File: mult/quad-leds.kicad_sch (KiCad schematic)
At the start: 14 parts, among them U5 LM324

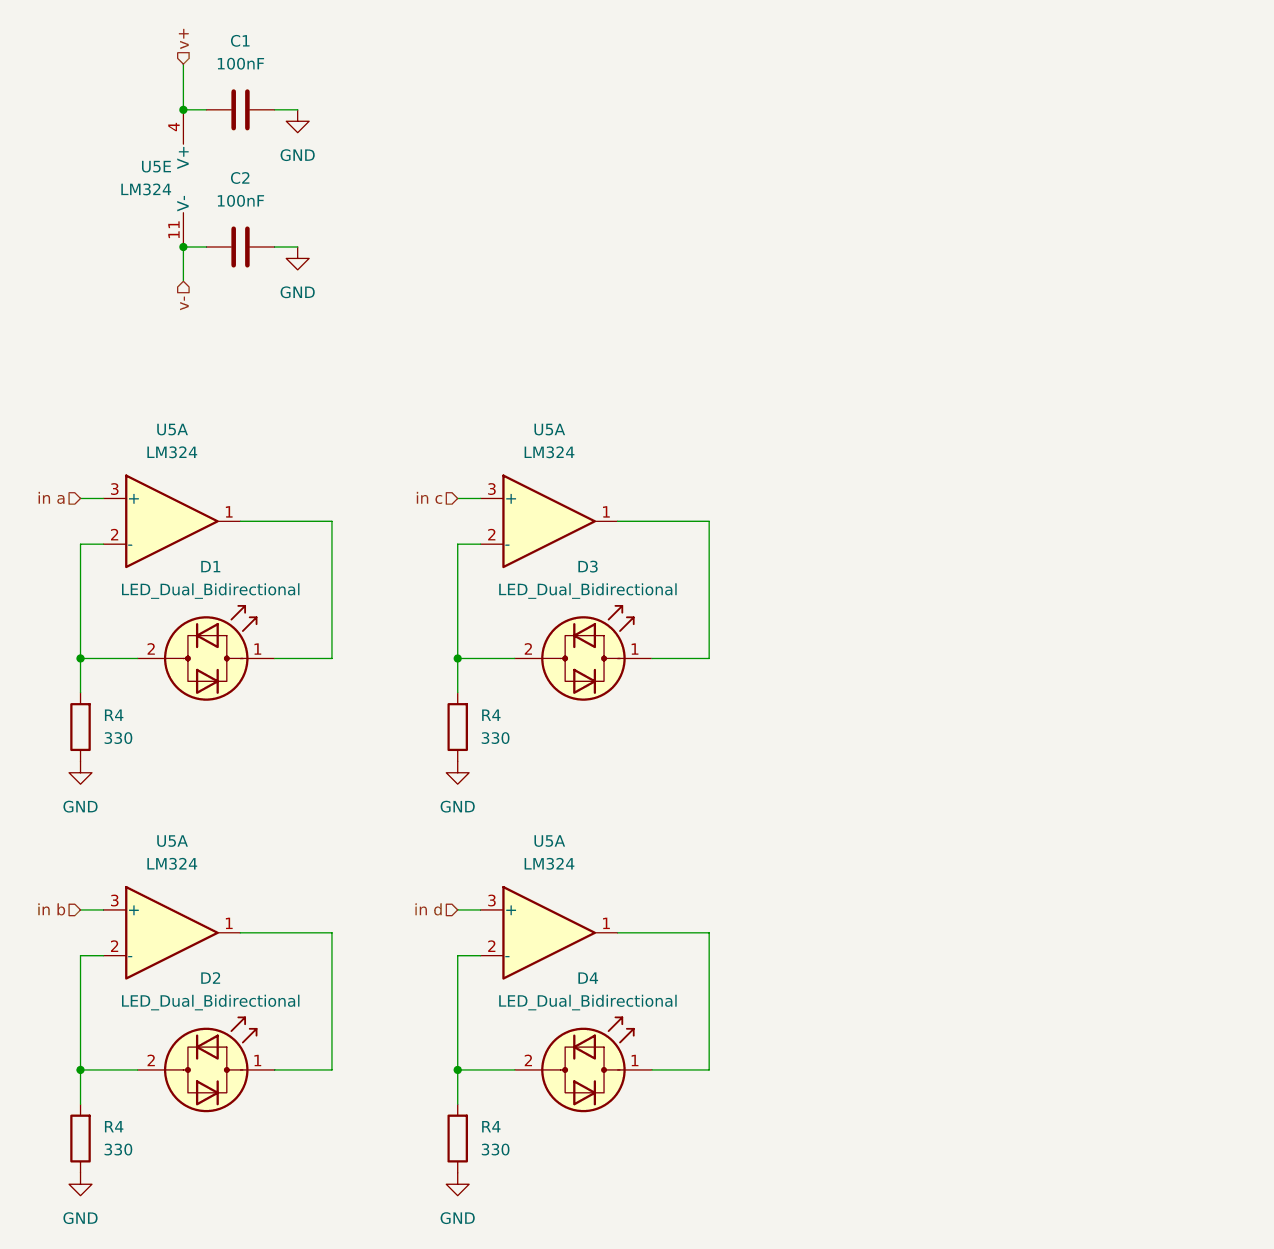
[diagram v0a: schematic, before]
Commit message: mult: Add LED TODOs, change resistor values to 680
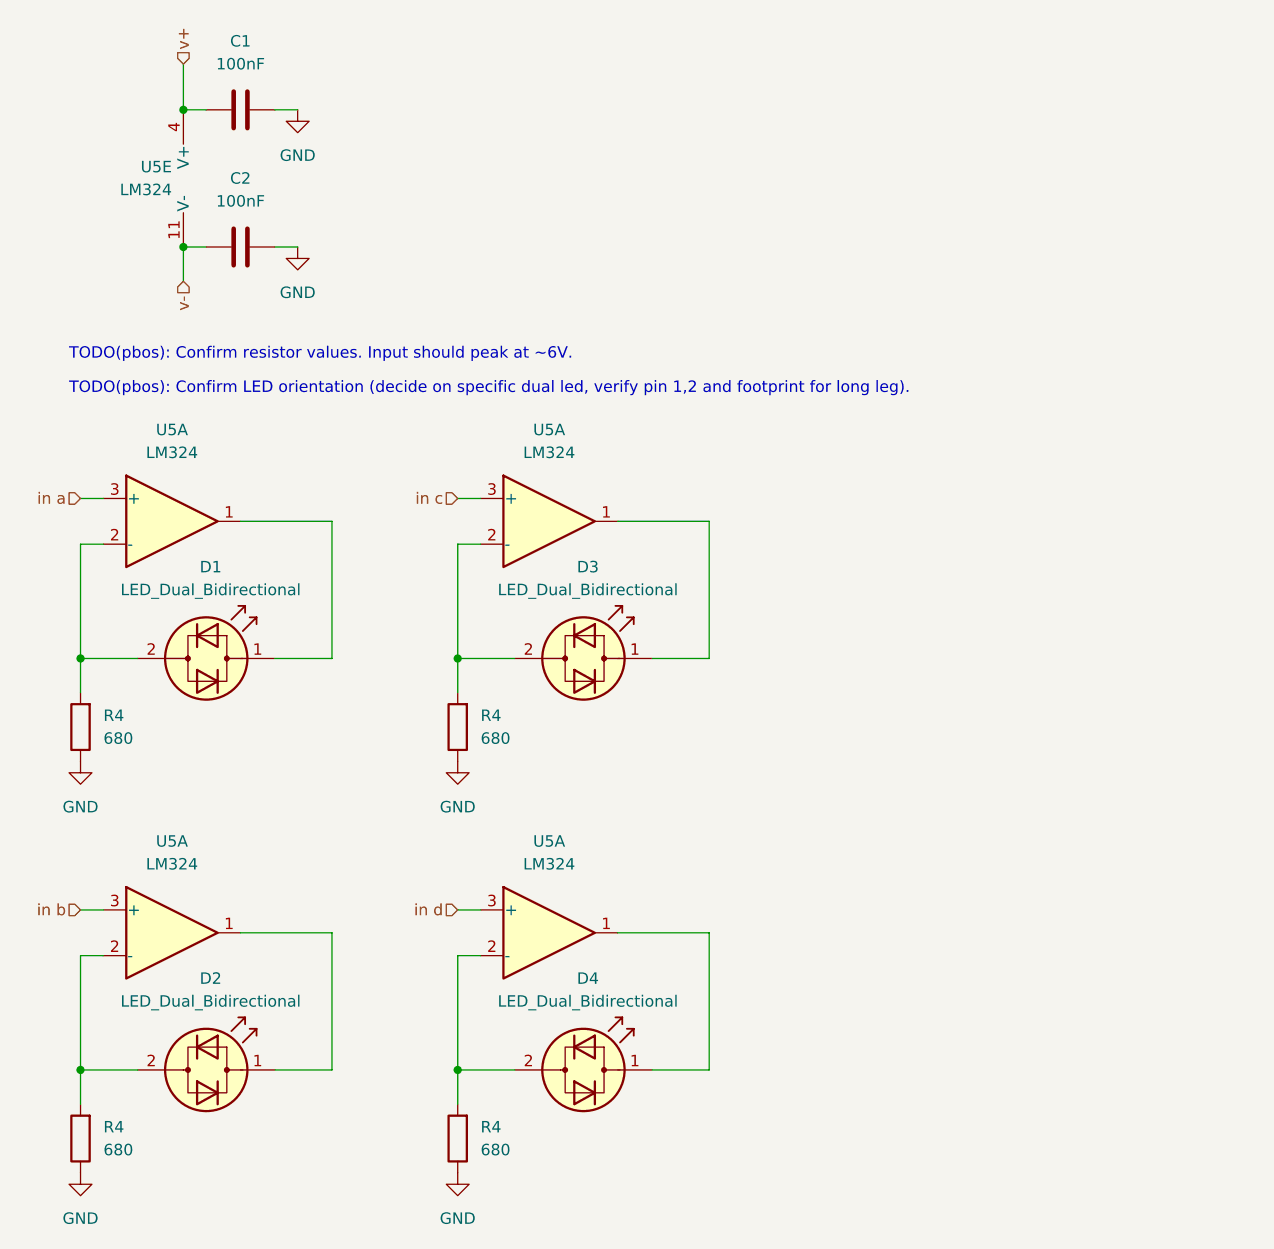
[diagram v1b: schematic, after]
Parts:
- R4: value 330 -> 680
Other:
- note added: "TODO(pbos): Confirm LED orientation (decide on specific dual led, verify pin 1,2 and footprint for long leg)."
- note added: "TODO(pbos): Confirm resistor values. Input should peak at ~6V."
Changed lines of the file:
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@@
     (stroke (width 0) (type default))
+  )
+  (text "TODO(pbos): Confirm LED orientation (decide on specific dual led, verify pin 1,2 and footprint for long leg)."
+    (at 78.74 73.66 0)
+    (effects (font (size 1.27 1.27)) (justify left bottom))
+  )
+  (text "TODO(pbos): Confirm resistor values. Input should peak at ~6V."
+    (at 78.74 69.85 0)
+    (effects (font (size 1.27 1.27)) (justify left bottom))
   )
   (hierarchical_label "in d" (shape input) (at 121.92 130.81 180) (fields_autoplaced)
@@
       (effects (font (size 1.27 1.27)) (justify right))
     )
-    (property "Value" "330" (at 82.55 157.48 0)
+    (property "Value" "680" (at 82.55 157.48 0)
       (effects (font (size 1.27 1.27)) (justify right))
     )
@@
       (effects (font (size 1.27 1.27)) (justify right))
     )
-    (property "Value" "330" (at 82.55 111.76 0)
+    (property "Value" "680" (at 82.55 111.76 0)
       (effects (font (size 1.27 1.27)) (justify right))
     )
@@
       (effects (font (size 1.27 1.27)) (justify right))
     )
-    (property "Value" "330" (at 124.46 157.48 0)
+    (property "Value" "680" (at 124.46 157.48 0)
       (effects (font (size 1.27 1.27)) (justify right))
     )
@@
       (effects (font (size 1.27 1.27)) (justify right))
     )
-    (property "Value" "330" (at 124.46 111.76 0)
-      (effects (font (size 1.27 1.27)) (justify right))
-    )
+    (property "Value" "680" (at 124.46 111.76 0)
+      (effects (font (size 1.27 1.27)) (justify right))
+    )

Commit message: mult: Add TSSOP footprint to LM324
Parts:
- U5: footprint (none) -> Package_SO:TSSOP-14_4.4x5mm_P0.65mm
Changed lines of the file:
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@@
       (effects (font (size 1.27 1.27)))
     )
-    (property "Footprint" "" (at 130.81 130.81 0)
+    (property "Footprint" "Package_SO:TSSOP-14_4.4x5mm_P0.65mm" (at 130.81 130.81 0)
       (effects (font (size 1.27 1.27)) hide)
     )
@@
       (effects (font (size 1.27 1.27)))
     )
-    (property "Footprint" "" (at 88.9 85.09 0)
+    (property "Footprint" "Package_SO:TSSOP-14_4.4x5mm_P0.65mm" (at 88.9 85.09 0)
       (effects (font (size 1.27 1.27)) hide)
     )
@@
       (effects (font (size 1.27 1.27)))
     )
-    (property "Footprint" "" (at 130.81 85.09 0)
+    (property "Footprint" "Package_SO:TSSOP-14_4.4x5mm_P0.65mm" (at 130.81 85.09 0)
       (effects (font (size 1.27 1.27)) hide)
     )
@@
       (effects (font (size 1.27 1.27)) (justify left))
     )
-    (property "Footprint" "" (at 90.17 46.99 0)
+    (property "Footprint" "Package_SO:TSSOP-14_4.4x5mm_P0.65mm" (at 90.17 46.99 0)
       (effects (font (size 1.27 1.27)) hide)
     )
@@
       (effects (font (size 1.27 1.27)))
     )
-    (property "Footprint" "" (at 88.9 130.81 0)
-      (effects (font (size 1.27 1.27)) hide)
-    )
+    (property "Footprint" "Package_SO:TSSOP-14_4.4x5mm_P0.65mm" (at 88.9 130.81 0)
+      (effects (font (size 1.27 1.27)) hide)
+    )

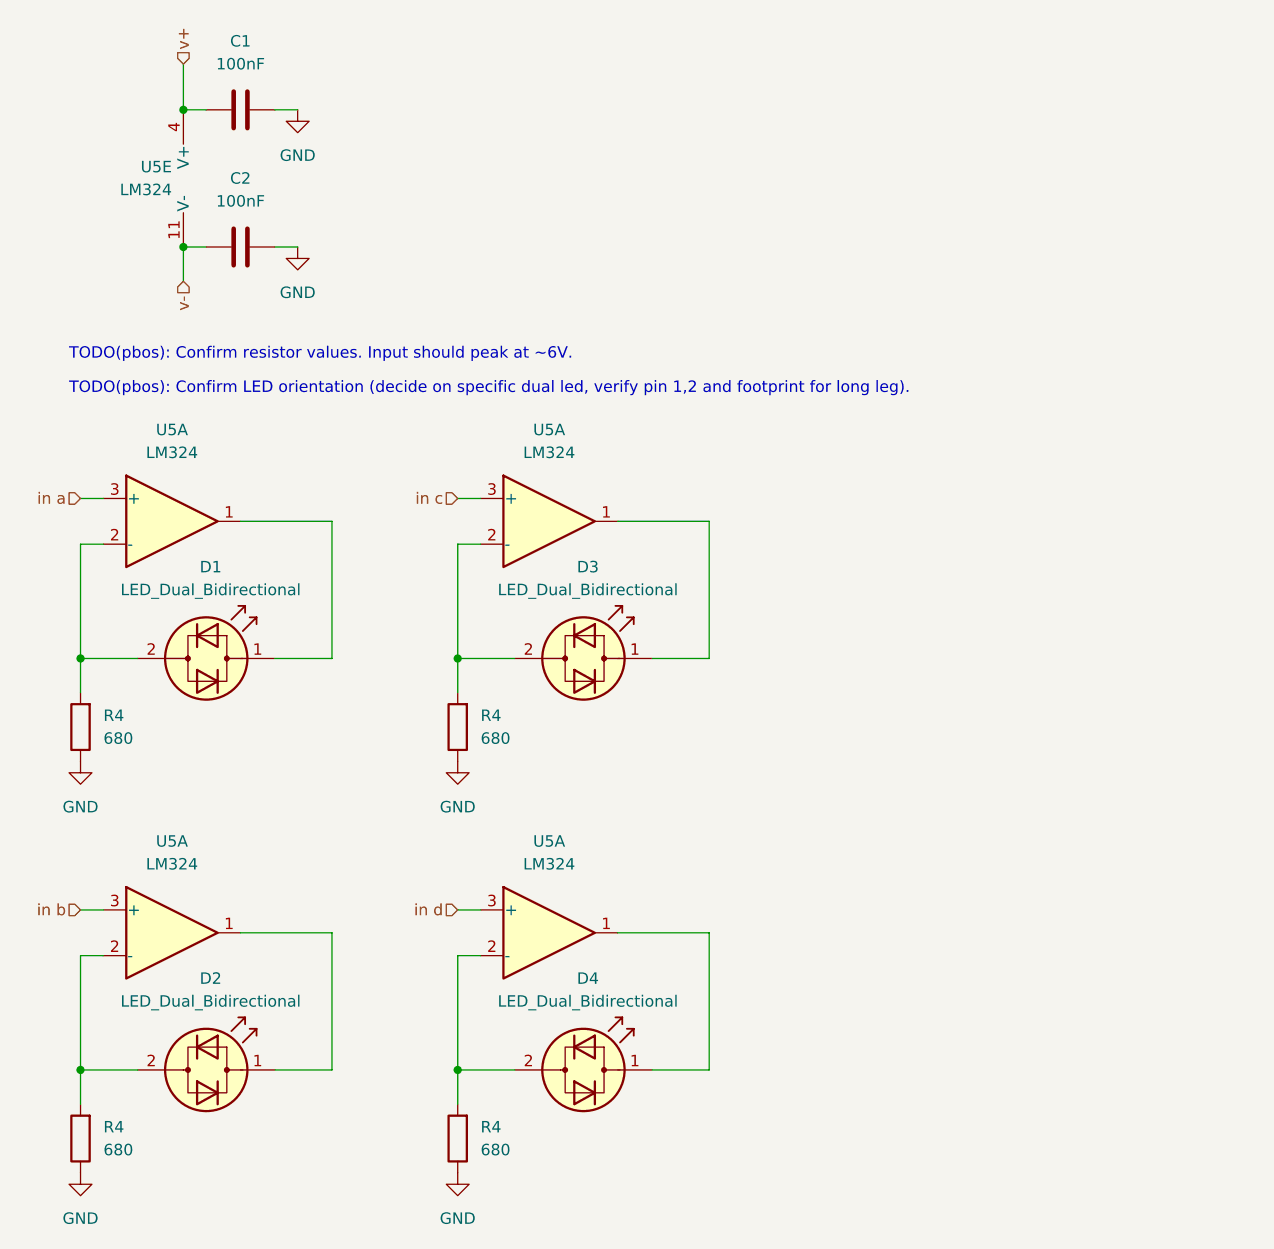
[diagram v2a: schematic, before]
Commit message: mult: Replace v+ and v- labels with VCC,VEE
This removes a lot of unnecessary wires as well. Also updating LED
resistors to 1k to match Mutable Instruments Links and resolving TODO.
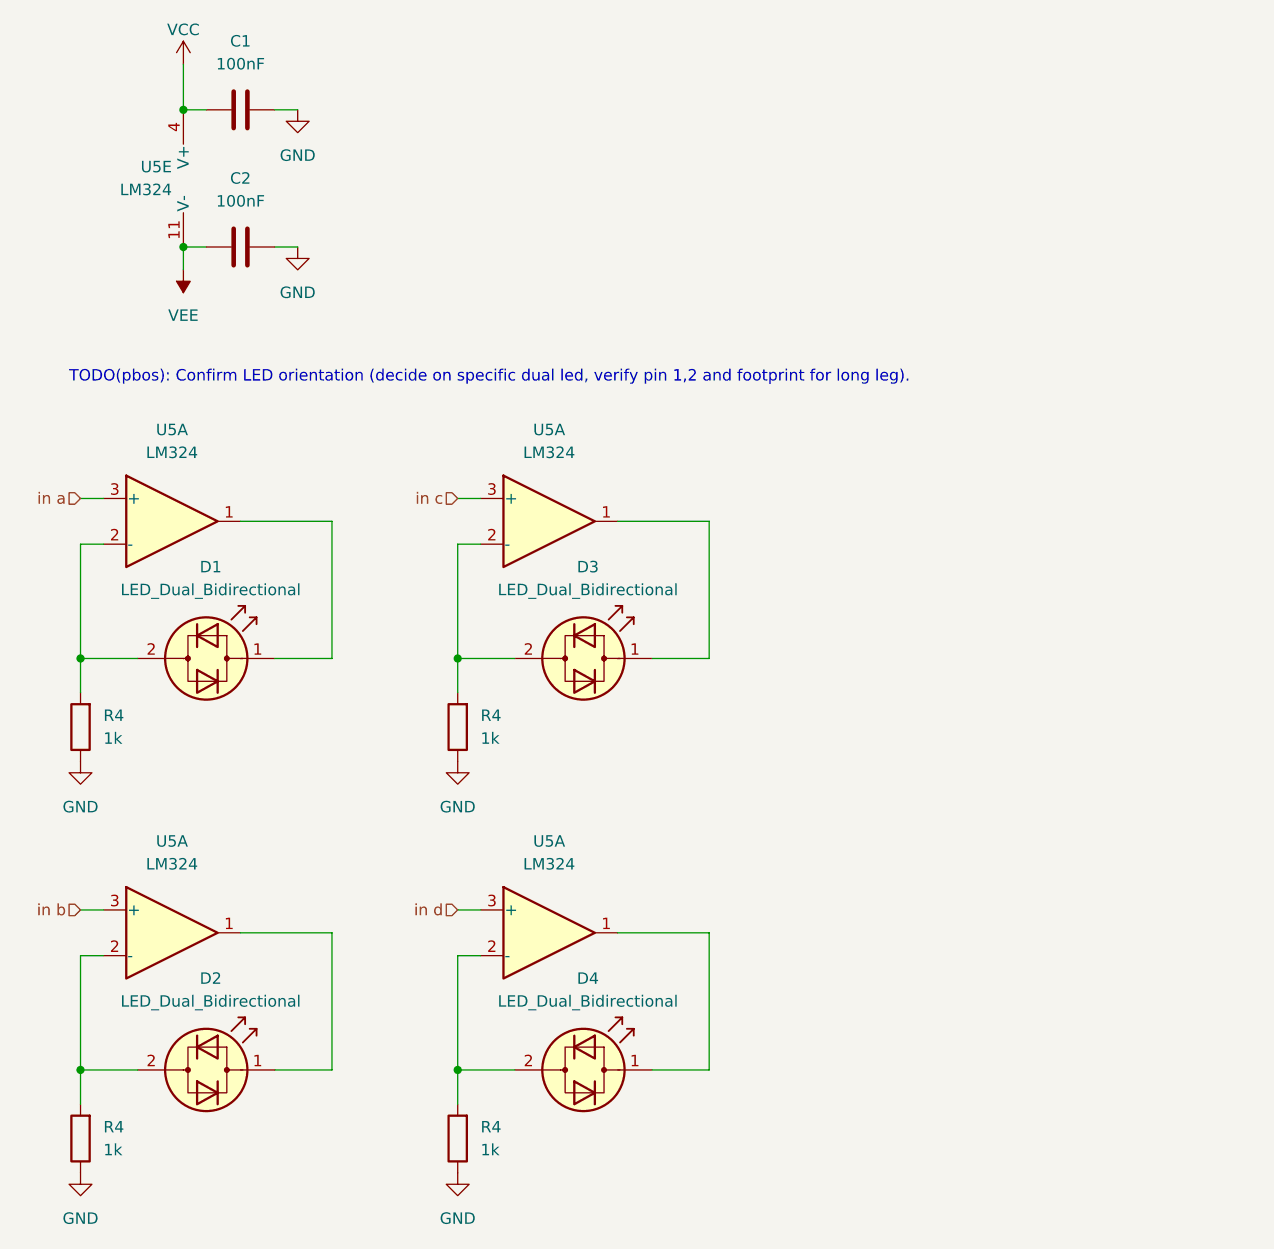
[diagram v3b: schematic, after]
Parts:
- R4: value 680 -> 1k
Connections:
- net v+ renamed VCC
- net v- renamed VEE
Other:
- note removed: "TODO(pbos): Confirm resistor values. Input should peak at ~6V."
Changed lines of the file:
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@@
     (stroke (width 0) (type default))
   )
-  (wire (pts (xy 91.44 60.96) (xy 91.44 57.15))
+  (wire (pts (xy 91.44 59.69) (xy 91.44 57.15))
     (stroke (width 0) (type default))
   )
@@
   )
   (text "TODO(pbos): Confirm LED orientation (decide on specific dual led, verify pin 1,2 and footprint for long leg)."
-    (at 78.74 73.66 0)
-    (effects (font (size 1.27 1.27)) (justify left bottom))
-  )
-  (text "TODO(pbos): Confirm resistor values. Input should peak at ~6V."
-    (at 78.74 69.85 0)
+    (at 78.74 72.39 0)
     (effects (font (size 1.27 1.27)) (justify left bottom))
   )
@@
   )
   (hierarchical_label "in c" (shape input) (at 121.92 85.09 180) (fields_autoplaced)
-    (effects (font (size 1.27 1.27)) (justify right))
-  )
-  (hierarchical_label "v+" (shape input) (at 91.44 36.83 90) (fields_autoplaced)
-    (effects (font (size 1.27 1.27)) (justify left))
-  )
-  (hierarchical_label "v-" (shape input) (at 91.44 60.96 270) (fields_autoplaced)
     (effects (font (size 1.27 1.27)) (justify right))
   )
@@
       (effects (font (size 1.27 1.27)) (justify right))
     )
-    (property "Value" "680" (at 82.55 157.48 0)
+    (property "Value" "1k" (at 82.55 157.48 0)
       (effects (font (size 1.27 1.27)) (justify right))
     )
@@
         (path "/0e98ec4b-b4c7-447c-abd7-a761177a7f67/41fcec89-2c3a-419b-9d1d-2962d3c6916c"
           (reference "D4") (unit 1)
+        )
+      )
+    )
+  )
+  (symbol (lib_id "power:VCC") (at 91.44 36.83 0) (unit 1)
+    (in_bom yes) (on_board yes) (dnp no)
+    (property "Reference" "#PWR053" (at 91.44 40.64 0)
+      (effects (font (size 1.27 1.27)) hide)
+    )
+    (property "Value" "VCC" (at 91.44 33.02 0)
+      (effects (font (size 1.27 1.27)))
+    )
+    (property "Footprint" "" (at 91.44 36.83 0)
+      (effects (font (size 1.27 1.27)) hide)
+    )
+    (property "Datasheet" "" (at 91.44 36.83 0)
+      (effects (font (size 1.27 1.27)) hide)
+    )
+    (pin "1")
+    (instances
+      (project "mult"
+        (path "/0e98ec4b-b4c7-447c-abd7-a761177a7f67/41fcec89-2c3a-419b-9d1d-2962d3c6916c"
+          (reference "#PWR053") (unit 1)
         )
       )
@@
       (effects (font (size 1.27 1.27)) (justify right))
     )
-    (property "Value" "680" (at 82.55 111.76 0)
+    (property "Value" "1k" (at 82.55 111.76 0)
       (effects (font (size 1.27 1.27)) (justify right))
     )
@@
       (effects (font (size 1.27 1.27)) (justify right))
     )
-    (property "Value" "680" (at 124.46 157.48 0)
+    (property "Value" "1k" (at 124.46 157.48 0)
       (effects (font (size 1.27 1.27)) (justify right))
     )
@@
       (effects (font (size 1.27 1.27)) (justify right))
     )
-    (property "Value" "680" (at 124.46 111.76 0)
+    (property "Value" "1k" (at 124.46 111.76 0)
       (effects (font (size 1.27 1.27)) (justify right))
     )
@@
         )
       )
+    )
+  )
+  (symbol (lib_id "power:VEE") (at 91.44 59.69 180) (unit 1)
+    (in_bom yes) (on_board yes) (dnp no) (fields_autoplaced)
+    (property "Reference" "#PWR054" (at 91.44 55.88 0)
+      (effects (font (size 1.27 1.27)) hide)
+    )
+    (property "Value" "VEE" (at 91.44 64.77 0)
+      (effects (font (size 1.27 1.27)))
+    )
+    (property "Footprint" "" (at 91.44 59.69 0)
+      (effects (font (size 1.27 1.27)) hide)
+    )
+    (property "Datasheet" "" (at 91.44 59.69 0)
+      (effects (font (size 1.27 1.27)) hide)
+    )
+    (pin "1")
+    (instances
+      (project "mult"
+        (path "/0e98ec4b-b4c7-447c-abd7-a761177a7f67/41fcec89-2c3a-419b-9d1d-2962d3c6916c"
+          (reference "#PWR054") (unit 1)
+        )
+      )
